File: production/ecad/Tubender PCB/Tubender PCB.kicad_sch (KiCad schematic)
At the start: 0 parts

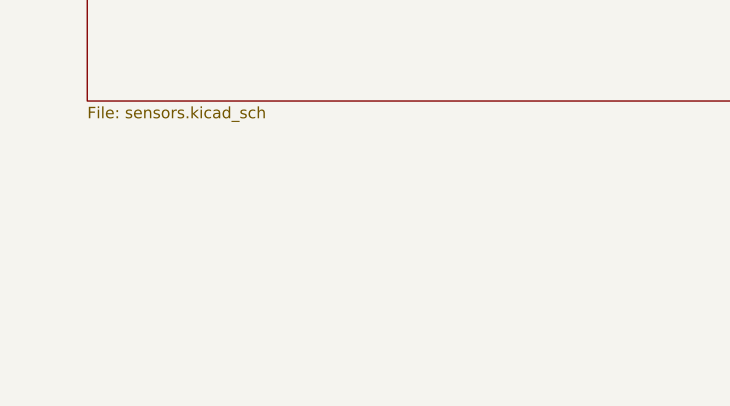
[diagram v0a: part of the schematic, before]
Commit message: Temp page added
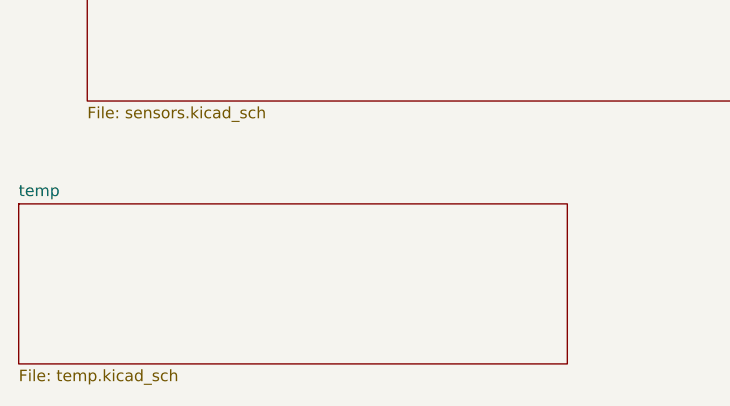
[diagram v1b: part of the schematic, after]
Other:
- added sheet temp (temp.kicad_sch)
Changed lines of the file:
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@@
+	)
+	(sheet
+		(at 43.18 173.99)
+		(size 60.96 17.78)
+		(fields_autoplaced yes)
+		(stroke
+			(width 0.1524)
+			(type solid)
+		)
+		(fill
+			(color 0 0 0 0.0000)
+		)
+		(property "Sheetname" "temp"
+			(at 43.18 173.2784 0)
+			(effects
+				(font
+					(size 1.27 1.27)
+				)
+				(justify left bottom)
+			)
+		)
+		(property "Sheetfile" "temp.kicad_sch"
+			(at 43.18 192.3546 0)
+			(effects
+				(font
+					(size 1.27 1.27)
+				)
+				(justify left top)
+			)
+		)
+		(instances
+			(project "Tubender PCB"
+				(path "/3e1aedd0-6089-4edb-92c7-0c31da2e7927"
+					(page "7")
+				)
+			)
+		)
 	)
 	(sheet

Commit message: final for rev 1
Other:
- removed sheet temp
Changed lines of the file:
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@@
-	)
-	(sheet
-		(at 43.18 173.99)
-		(size 60.96 17.78)
-		(fields_autoplaced yes)
-		(stroke
-			(width 0.1524)
-			(type solid)
-		)
-		(fill
-			(color 0 0 0 0.0000)
-		)
-		(property "Sheetname" "temp"
-			(at 43.18 173.2784 0)
-			(effects
-				(font
-					(size 1.27 1.27)
-				)
-				(justify left bottom)
-			)
-		)
-		(property "Sheetfile" "temp.kicad_sch"
-			(at 43.18 192.3546 0)
-			(effects
-				(font
-					(size 1.27 1.27)
-				)
-				(justify left top)
-			)
-		)
-		(instances
-			(project "Tubender PCB"
-				(path "/3e1aedd0-6089-4edb-92c7-0c31da2e7927"
-					(page "7")
-				)
-			)
-		)
 	)
 	(sheet
